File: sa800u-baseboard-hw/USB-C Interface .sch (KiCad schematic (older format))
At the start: 21 parts, among them J1 MUSBRM1C1M0, U2 TS3USB30EDGSR

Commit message: Review - Add geeral remarks
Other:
- note added: "REMARK: USE _N instead of _M ( Kicad can't recognize _M)"
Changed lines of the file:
@@
 Text Notes 7500 1050 0    50   ~ 0
 This should be optional,\nhard to get component and\nnot necessary.
+Text Notes 6075 3325 0    50   ~ 0
+REMARK: USE _N instead of _M ( Kicad can't recognize _M)
 $EndSCHEMATC

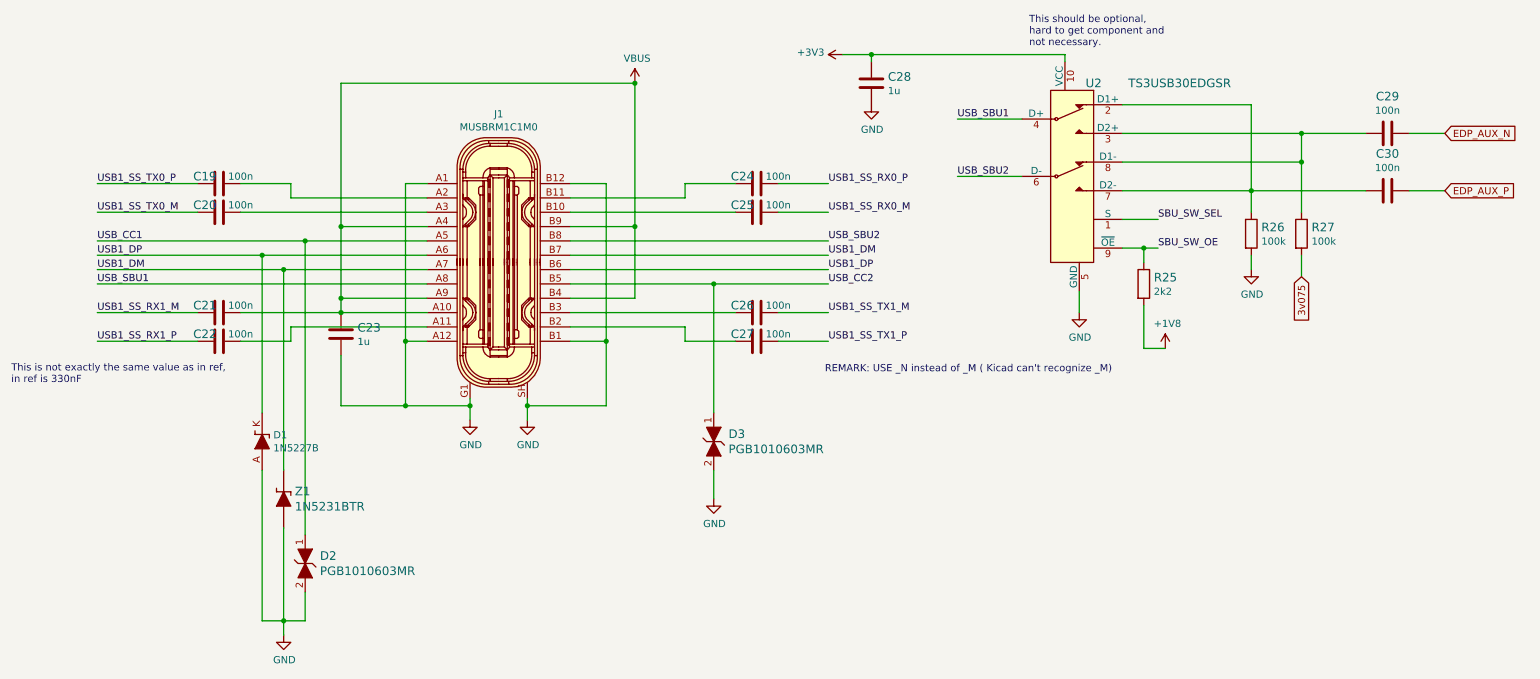
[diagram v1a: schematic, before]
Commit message: fixed labels for differential pairs
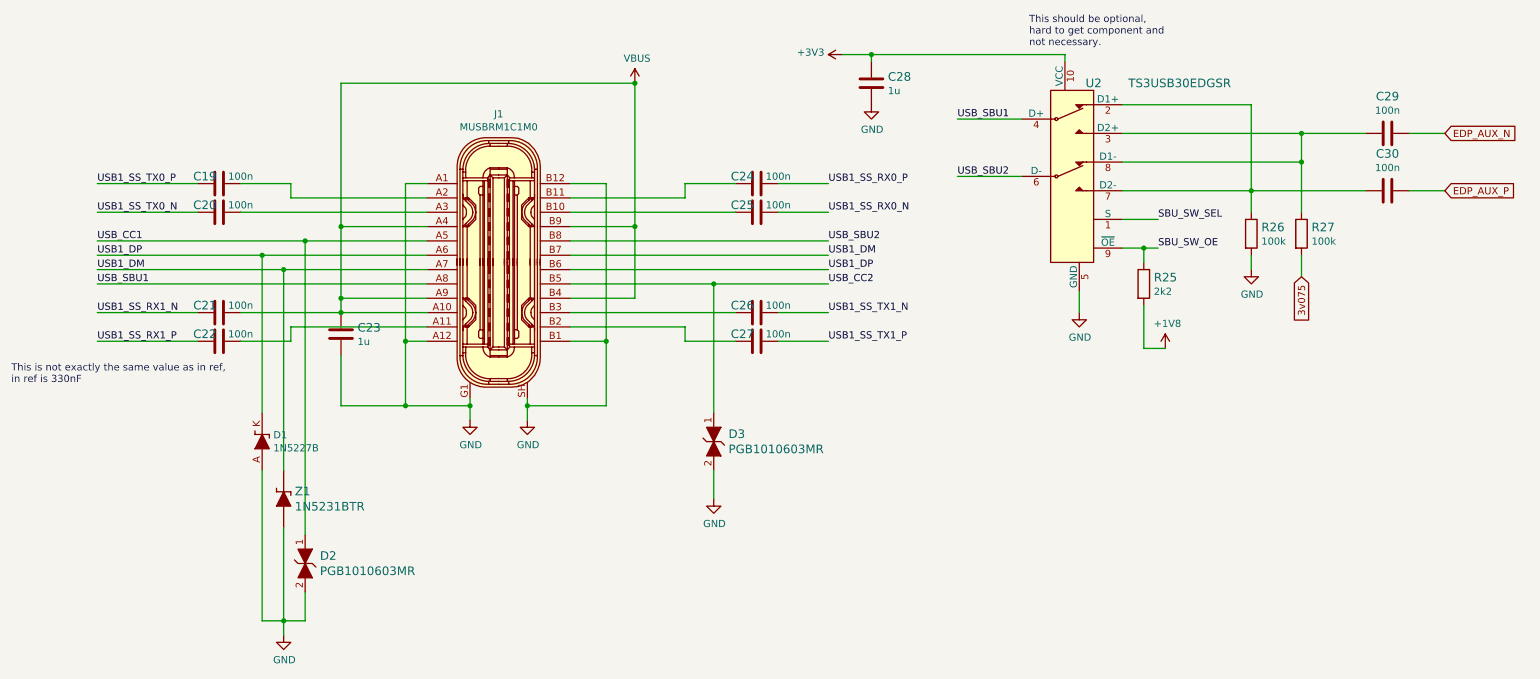
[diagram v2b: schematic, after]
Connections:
- net USB1_SS_RX0_M renamed USB1_SS_RX0_N
- net USB1_SS_RX1_M renamed USB1_SS_RX1_N
- net USB1_SS_TX0_M renamed USB1_SS_TX0_N
- net USB1_SS_TX1_M renamed USB1_SS_TX1_N
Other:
- note removed: "REMARK: USE _N instead of _M ( Kicad can't recognize _M)"
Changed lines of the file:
@@
 USB1_SS_TX0_P
 Text Label 1000 2200 0    50   ~ 0
-USB1_SS_TX0_M
+USB1_SS_TX0_N
 Wire Wire Line
 	1000 2000 1700 2000
@@
 	1700 3100 1000 3100
 Text Label 1000 2900 0    50   ~ 0
-USB1_SS_RX1_M
+USB1_SS_RX1_N
 Text Label 1000 3100 0    50   ~ 0
 USB1_SS_RX1_P
@@
 USB1_SS_RX0_P
 Text Label 6100 2200 0    50   ~ 0
-USB1_SS_RX0_M
+USB1_SS_RX0_N
 Wire Wire Line
 	4300 2300 4750 2300
@@
 	5750 3100 6100 3100
 Text Label 6100 2900 0    50   ~ 0
-USB1_SS_TX1_M
+USB1_SS_TX1_N
 Text Label 6100 3100 0    50   ~ 0
 USB1_SS_TX1_P
@@
 Text Notes 7500 1050 0    50   ~ 0
 This should be optional,\nhard to get component and\nnot necessary.
-Text Notes 6075 3325 0    50   ~ 0
-REMARK: USE _N instead of _M ( Kicad can't recognize _M)
 $EndSCHEMATC

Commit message: introducing minor genreal improvements
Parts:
- removed C21, C22: C_100n_0402, antmicro-footprints:0402-cap, symbol antmicroCapacitors0402:C_100n_0402
- added C? (x2): C_330n_0603, antmicro-footprints:0603-res, symbol antmicroCapacitors0603:C_330n_0603
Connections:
- net USB1_SS_RX1_N: now also C?.2
- net USB1_SS_RX1_P: now also C?.2
- net VBUS: now also C?.1
- net at J1.A11: now also C?.1
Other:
- note removed: "This is not exactly the same value as in ref,\nin ref is 330nF"
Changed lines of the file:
@@
 Wire Wire Line
 	2350 3100 2000 3100
-$Comp
-L antmicroCapacitors0402:C_100n_0402 C21
-U 1 1 61B0AD05
-P 1850 2900
-F 0 "C21" V 1800 2800 60  0000 C CNN
-F 1 "C_100n_0402" H 1850 2750 60  0001 C CNN
-F 2 "antmicro-footprints:0402-cap" H 2050 3100 60  0001 L CNN
-F 3 "" H 1850 2900 50  0001 C CNN
-F 4 "Walsin" H 2050 3300 60  0001 L CNN "Manufacturer"
-F 5 "0402X104K6R3CT" H 2050 3200 60  0001 L CNN "MPN"
-F 6 "100n" V 1800 3050 50  0000 C CNN "Val"
-	1    1850 2900
-	0    1    1    0
-$EndComp
-$Comp
-L antmicroCapacitors0402:C_100n_0402 C22
-U 1 1 61B0BA57
-P 1850 3100
-F 0 "C22" V 1800 3000 60  0000 C CNN
-F 1 "C_100n_0402" H 1850 2950 60  0001 C CNN
-F 2 "antmicro-footprints:0402-cap" H 2050 3300 60  0001 L CNN
-F 3 "" H 1850 3100 50  0001 C CNN
-F 4 "Walsin" H 2050 3500 60  0001 L CNN "Manufacturer"
-F 5 "0402X104K6R3CT" H 2050 3400 60  0001 L CNN "MPN"
-F 6 "100n" V 1800 3250 50  0000 C CNN "Val"
-	1    1850 3100
-	0    1    1    0
-$EndComp
-Text Notes 400  3400 0    50   ~ 0
-This is not exactly the same value as in ref,\nin ref is 330nF
-Wire Wire Line
-	1700 2900 1000 2900
 Wire Wire Line
 	1700 3100 1000 3100
@@
 Text Notes 7500 1050 0    50   ~ 0
 This should be optional,\nhard to get component and\nnot necessary.
+Wire Wire Line
+	1700 2900 1000 2900
+$Comp
+L antmicroCapacitors0603:C_330n_0603 C?
+U 1 1 61B288A3
+P 1850 2900
+F 0 "C?" V 1800 2750 60  0000 C CNN
+F 1 "C_330n_0603" H 1850 2750 60  0001 C CNN
+F 2 "antmicro-footprints:0603-res" H 2050 3100 60  0001 L CNN
+F 3 "https://pl.mouser.com/datasheet/2/427/VISH_S_A0008004061_1-2570247.pdf" H 1850 2900 50  0001 C CNN
+F 4 "Vishay" H 2050 3300 60  0001 L CNN "Manufacturer"
+F 5 "VJ0603A331JXBAC" H 2050 3200 60  0001 L CNN "MPN"
+F 6 "330n" V 1800 3100 50  0000 C CNN "Val"
+	1    1850 2900
+	0    1    1    0
+$EndComp
+$Comp
+L antmicroCapacitors0603:C_330n_0603 C?
+U 1 1 61B290D9
+P 1850 3100
+F 0 "C?" V 1800 2950 60  0000 C CNN
+F 1 "C_330n_0603" H 1850 2950 60  0001 C CNN
+F 2 "antmicro-footprints:0603-res" H 2050 3300 60  0001 L CNN
+F 3 "https://pl.mouser.com/datasheet/2/427/VISH_S_A0008004061_1-2570247.pdf" H 1850 3100 50  0001 C CNN
+F 4 "Vishay" H 2050 3500 60  0001 L CNN "Manufacturer"
+F 5 "VJ0603A331JXBAC" H 2050 3400 60  0001 L CNN "MPN"
+F 6 "330n" V 1800 3300 50  0000 C CNN "Val"
+	1    1850 3100
+	0    1    1    0
+$EndComp
 $EndSCHEMATC

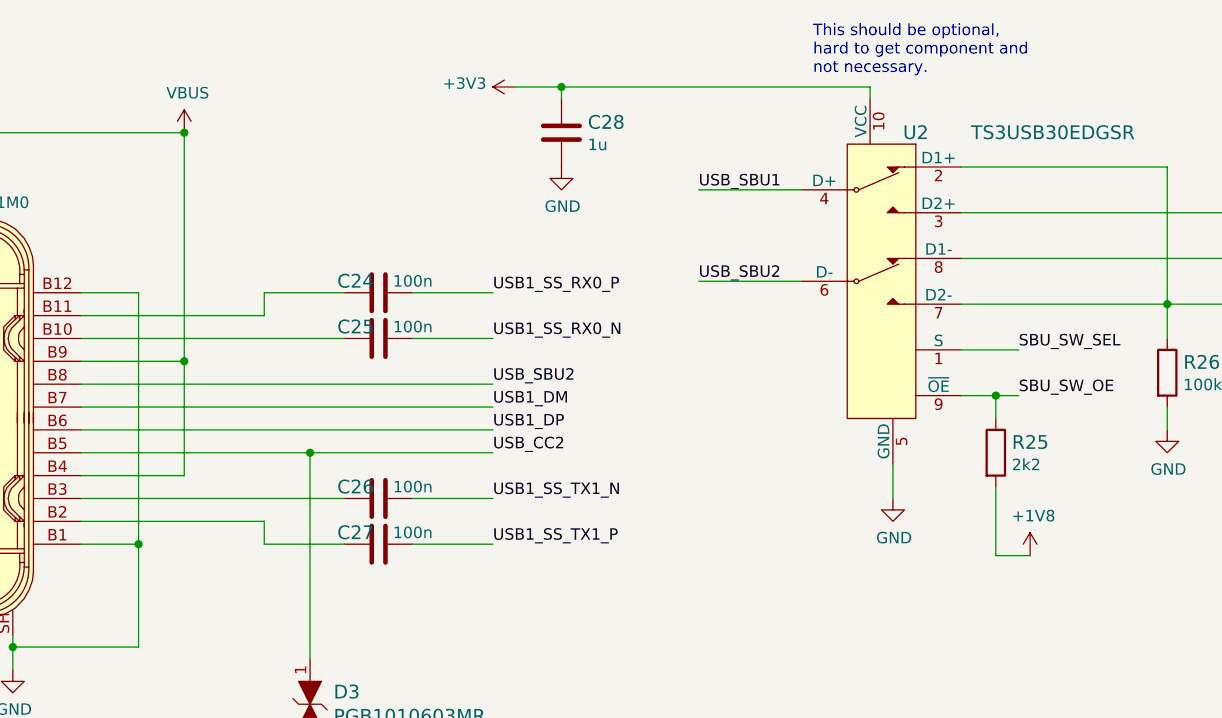
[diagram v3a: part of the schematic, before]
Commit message: fixed / unified power labels
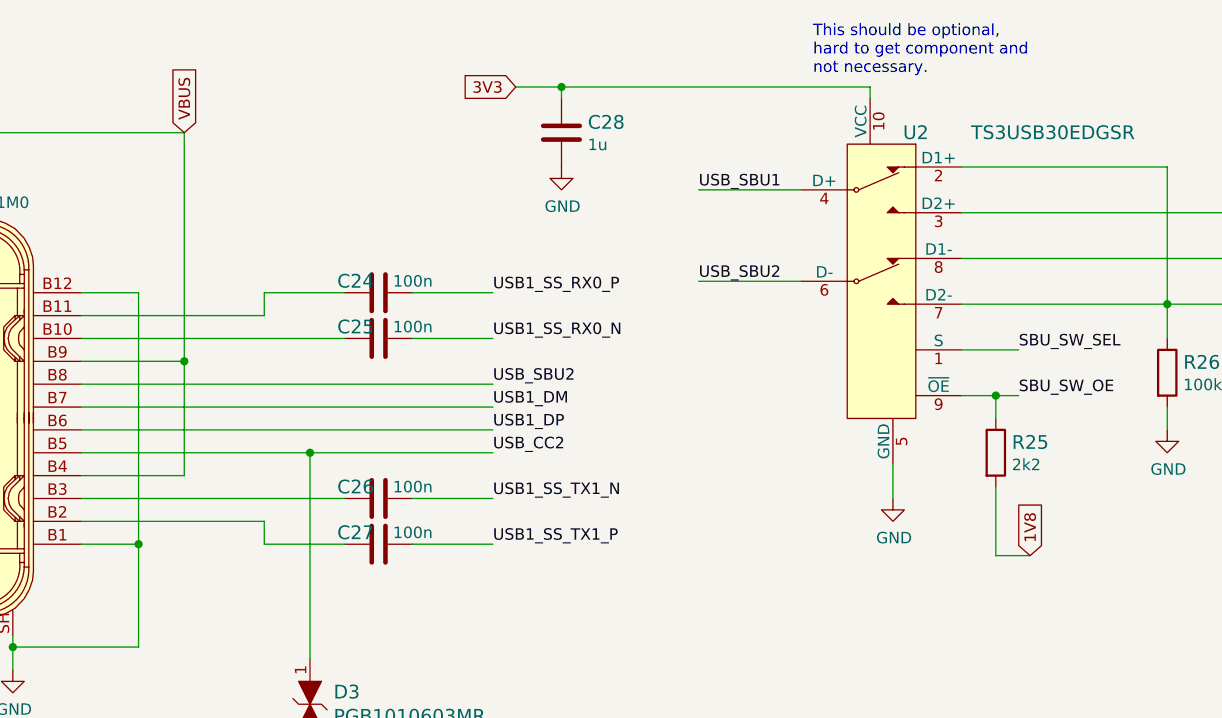
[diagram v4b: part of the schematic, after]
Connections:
- net +1V8 renamed 1V8
- net +3V3 renamed 3V3
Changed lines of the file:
@@
 Wire Wire Line
 	7750 1150 7750 1100
-$Comp
-L power:+3V3 #PWR021
-U 1 1 61A4DDE1
-P 6200 1100
-F 0 "#PWR021" H 6200 950 50  0001 C CNN
-F 1 "+3V3" V 6215 1228 50  0000 L CNN
-F 2 "" H 6200 1100 50  0001 C CNN
-F 3 "" H 6200 1100 50  0001 C CNN
-	1    6200 1100
-	0    -1   -1   0
-$EndComp
 Text Label 7000 1550 0    50   ~ 0
 USB_SBU1
@@
 	0    1    1    0
 $EndComp
-$Comp
-L power:+1V8 #PWR024
-U 1 1 61A7947B
-P 8450 3150
-F 0 "#PWR024" H 8450 3000 50  0001 C CNN
-F 1 "+1V8" H 8465 3323 50  0000 C CNN
-F 2 "" H 8450 3150 50  0001 C CNN
-F 3 "" H 8450 3150 50  0001 C CNN
-	1    8450 3150
-	1    0    0    -1
-$EndComp
 Wire Wire Line
 	8300 3150 8450 3150
@@
 Wire Wire Line
 	10150 2050 10400 2050
-$Comp
-L power:VBUS #PWR019
-U 1 1 61AB1226
-P 4750 1300
-F 0 "#PWR019" H 4750 1150 50  0001 C CNN
-F 1 "VBUS" H 4765 1473 50  0000 C CNN
-F 2 "" H 4750 1300 50  0001 C CNN
-F 3 "" H 4750 1300 50  0001 C CNN
-	1    4750 1300
-	1    0    0    -1
-$EndComp
 Wire Wire Line
 	3300 2800 2700 2800
@@
 Wire Wire Line
 	4750 2800 4300 2800
-Connection ~ 4750 1300
 $Comp
 L antmicroCapacitors0402:C_1u_0402 C23
@@
 	0    1    1    0
 $EndComp
+Text GLabel 4750 1300 1    50   Input ~ 0
+VBUS
+Text GLabel 6200 1100 0    50   Input ~ 0
+3V3
+Text GLabel 8450 3150 1    50   Input ~ 0
+1V8
 $EndSCHEMATC

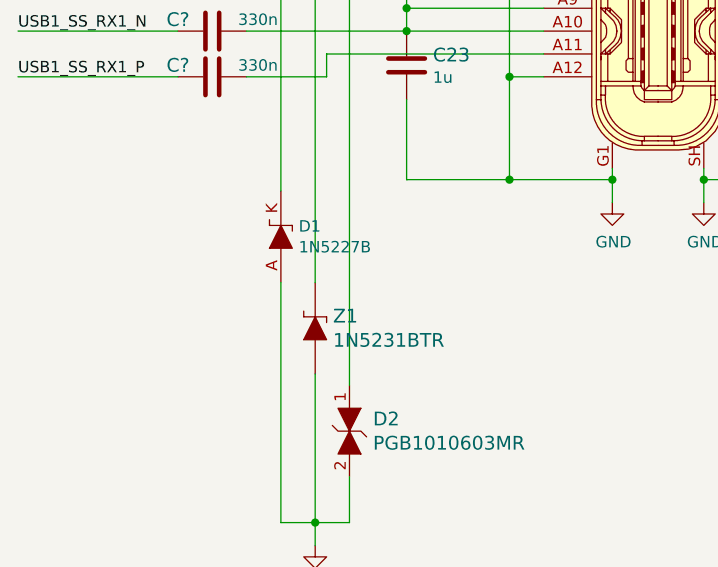
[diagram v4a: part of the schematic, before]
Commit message: flattenning directory
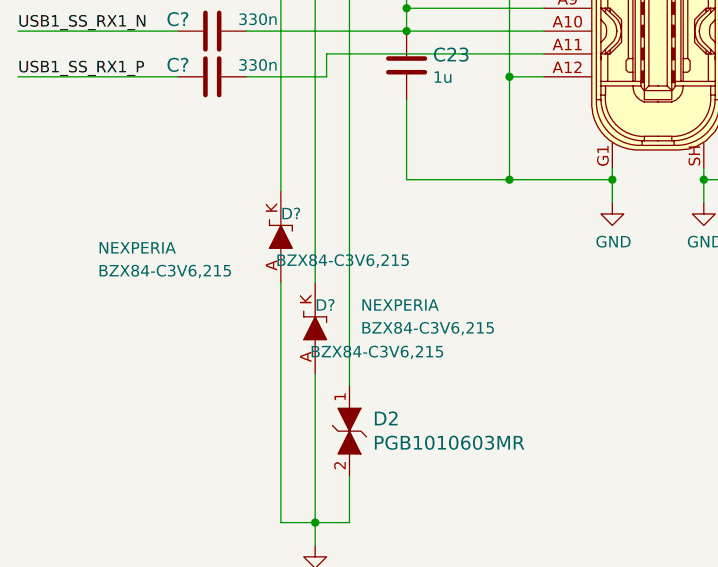
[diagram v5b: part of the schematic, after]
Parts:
- removed D1: 1N5227B, symbol ZenerDiode:1N5227B
- removed Z1: 1N5231BTR, antmicro-footprints:DO-35, symbol antmicroDiodesZenerSingle:1N5231BTR
- added D? (x2): BZX84-C3V6,215, antmicro-footprints:SOT95P230X110-3N, symbol antmicroDiodesZenerSingle:BZX84-C3V6,215
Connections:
- net GND: now also D?.A, D?.A
- net USB1_DM: now also D?.K
- net USB1_DP: now also D?.K
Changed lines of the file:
@@
 $Descr A4 11693 8268
 encoding utf-8
-Sheet 5 7
+Sheet 4 7
 Title ""
 Date ""
@@
 	0    1    1    0
 $EndComp
-$Comp
-L antmicroDiodesZenerSingle:1N5231BTR Z1
-U 1 1 61B3339A
-P 2300 4200
-F 0 "Z1" V 2353 4122 60  0000 R CNN
-F 1 "1N5231BTR" V 2247 4122 60  0000 R CNN
-F 2 "antmicro-footprints:DO-35" H 2500 4400 60  0001 L CNN
-F 3 "https://www.onsemi.com/pub/Collateral/1N5221B-D.PDF" H 2500 4500 60  0001 L CNN
-F 4 "1N5231BTR" H 2500 4700 60  0001 L CNN "MPN"
-F 5 "ON Semiconductor" H 2500 5300 60  0001 L CNN "Manufacturer"
-	1    2300 4200
-	0    -1   -1   0
-$EndComp
-$Comp
-L ZenerDiode:1N5227B D1
-U 1 1 61B35D92
-P 2150 3800
-F 0 "D1" V 2196 3722 50  0000 R CNN
-F 1 "1N5227B" V 2105 3722 50  0000 R CNN
-F 2 "" H 2150 3950 50  0001 C CNN
-F 3 "" H 2150 3950 50  0001 C CNN
-	1    2150 3800
-	0    -1   -1   0
-$EndComp
 Wire Wire Line
 	2450 2400 2450 4450
@@
 Text GLabel 8450 3150 1    50   Input ~ 0
 1V8
+$Comp
+L antmicroDiodesZenerSingle:BZX84-C3V6,215 D?
+U 1 1 61A2E749
+P 2300 4200
+F 0 "D?" V 2400 4200 50  0000 R CNN
+F 1 "BZX84-C3V6,215" V 2196 4222 50  0000 R CNN
+F 2 "antmicro-footprints:SOT95P230X110-3N" H 2150 4400 50  0001 C CNN
+F 3 "https://www.farnell.com/datasheets/1808429.pdf" H 2150 4400 50  0001 C CNN
+F 4 "BZX84-C3V6,215" V 2300 4000 50  0000 R CNN "MPN"
+F 5 "NEXPERIA" V 2400 4000 50  0000 R CNN "Manufacturer"
+	1    2300 4200
+	0    -1   -1   0
+$EndComp
+$Comp
+L antmicroDiodesZenerSingle:BZX84-C3V6,215 D?
+U 1 1 61A30594
+P 2150 3800
+F 0 "D?" V 2250 3800 50  0000 R CNN
+F 1 "BZX84-C3V6,215" V 2046 3822 50  0000 R CNN
+F 2 "antmicro-footprints:SOT95P230X110-3N" H 2000 4000 50  0001 C CNN
+F 3 "https://www.farnell.com/datasheets/1808429.pdf" H 2000 4000 50  0001 C CNN
+F 4 "BZX84-C3V6,215" V 2000 4600 50  0000 R CNN "MPN"
+F 5 "NEXPERIA" V 2100 4600 50  0000 R CNN "Manufacturer"
+	1    2150 3800
+	0    -1   -1   0
+$EndComp
 $EndSCHEMATC
